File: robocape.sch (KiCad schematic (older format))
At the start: 16 parts

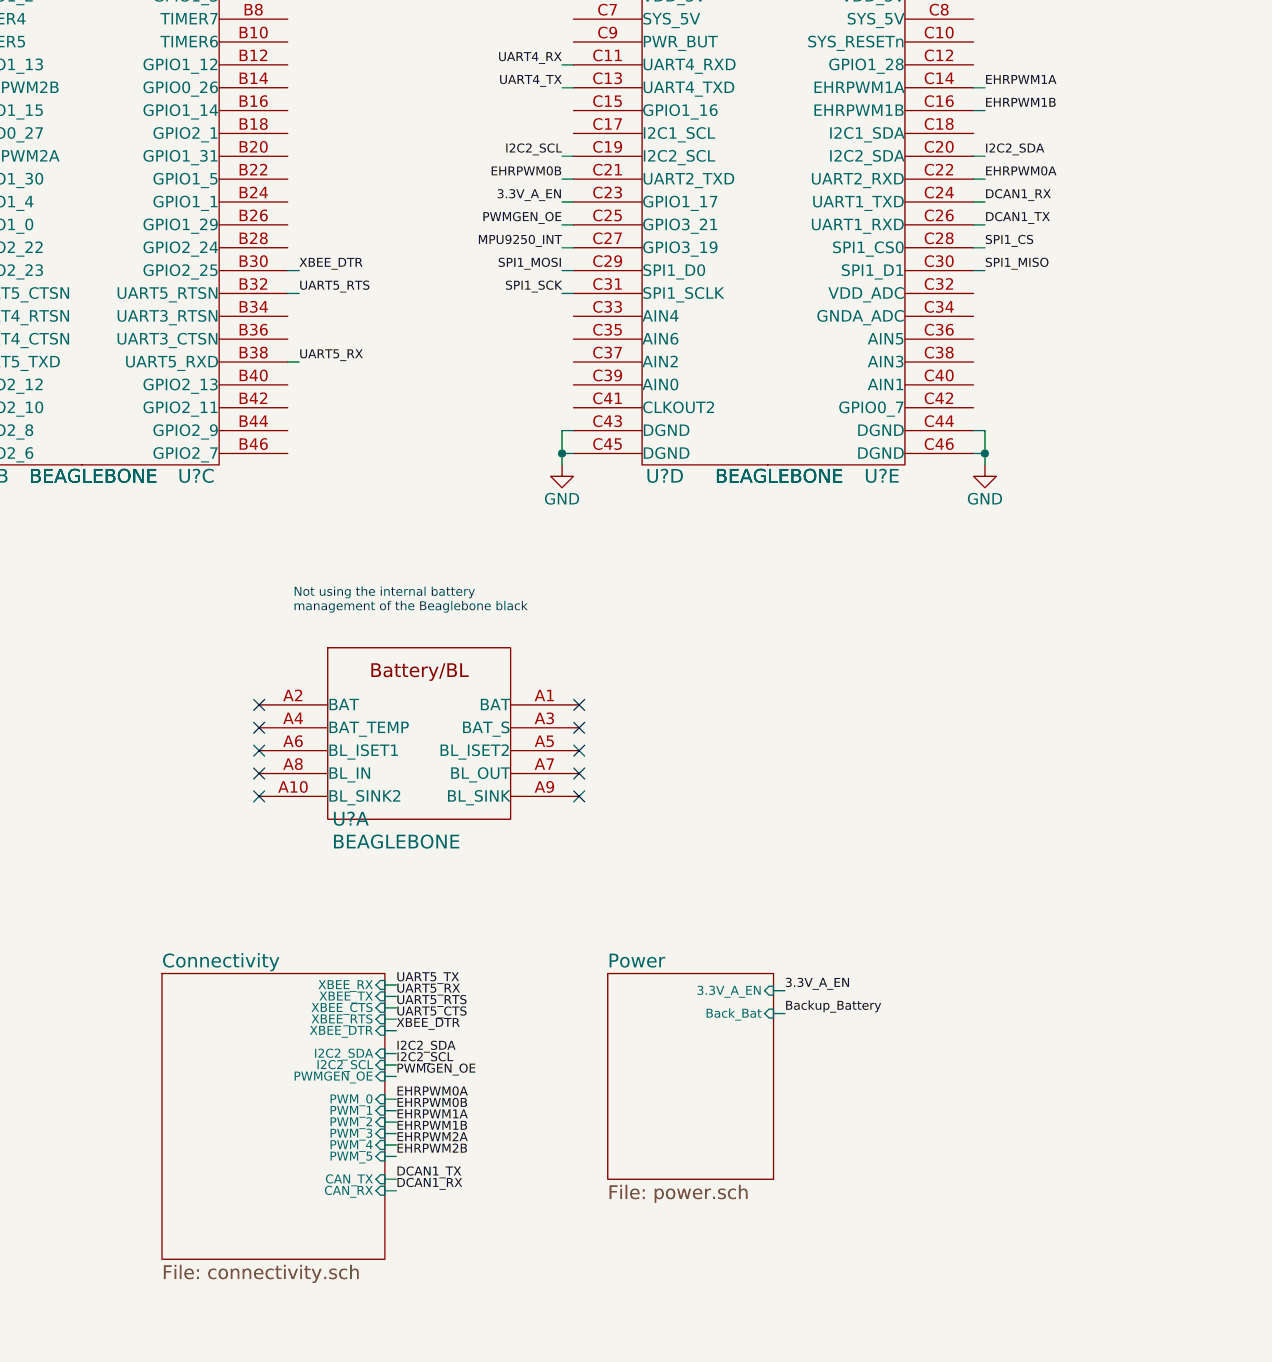
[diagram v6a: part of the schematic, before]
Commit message: Schematics: Additional connectors (ADC, I2C, UART)
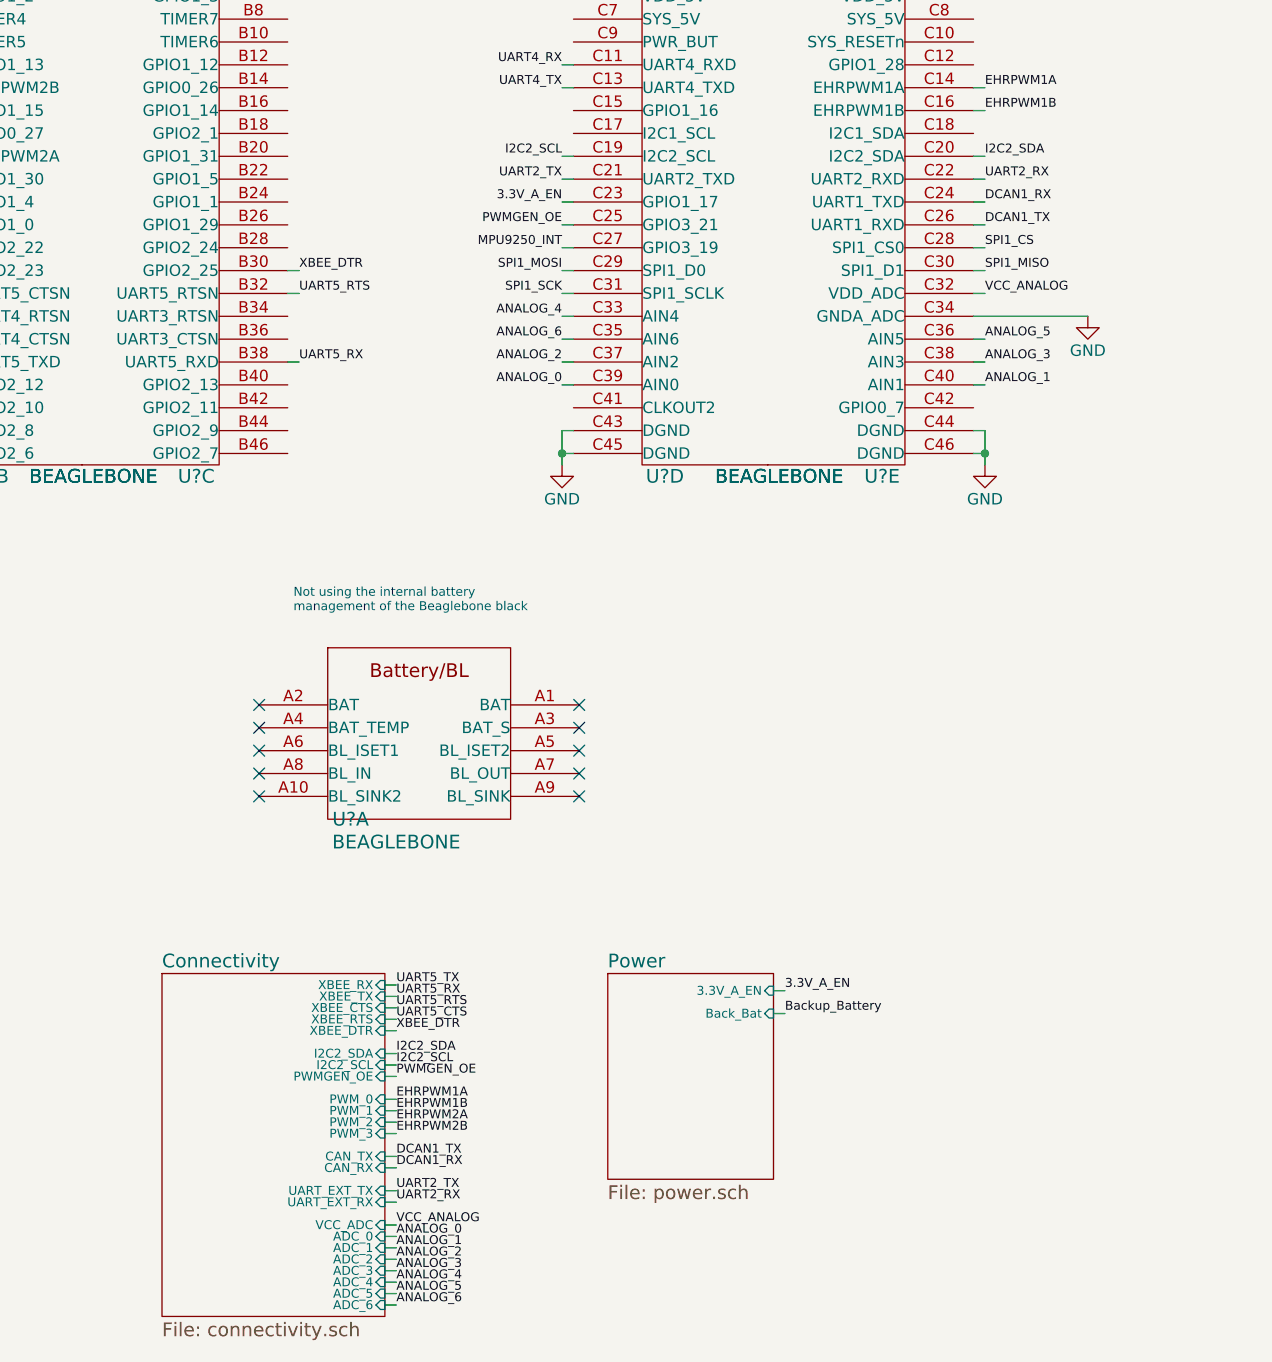
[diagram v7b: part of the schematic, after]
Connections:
- net GND: now also U?.C34 (GNDA_ADC)
- net ANALOG_4: now reaches U?.C33 (AIN4)
- net ANALOG_6: now reaches U?.C35 (AIN6)
- net ANALOG_2: now reaches U?.C37 (AIN2)
- net ANALOG_0: now reaches U?.C39 (AIN0)
- net VCC_ANALOG: now reaches U?.C32 (VDD_ADC)
- net ANALOG_5: now reaches U?.C36 (AIN5)
- net ANALOG_3: now reaches U?.C38 (AIN3)
- net ANALOG_1: now reaches U?.C40 (AIN1)
- net EHRPWM0A renamed UART2_RX
- net EHRPWM0B renamed UART2_TX

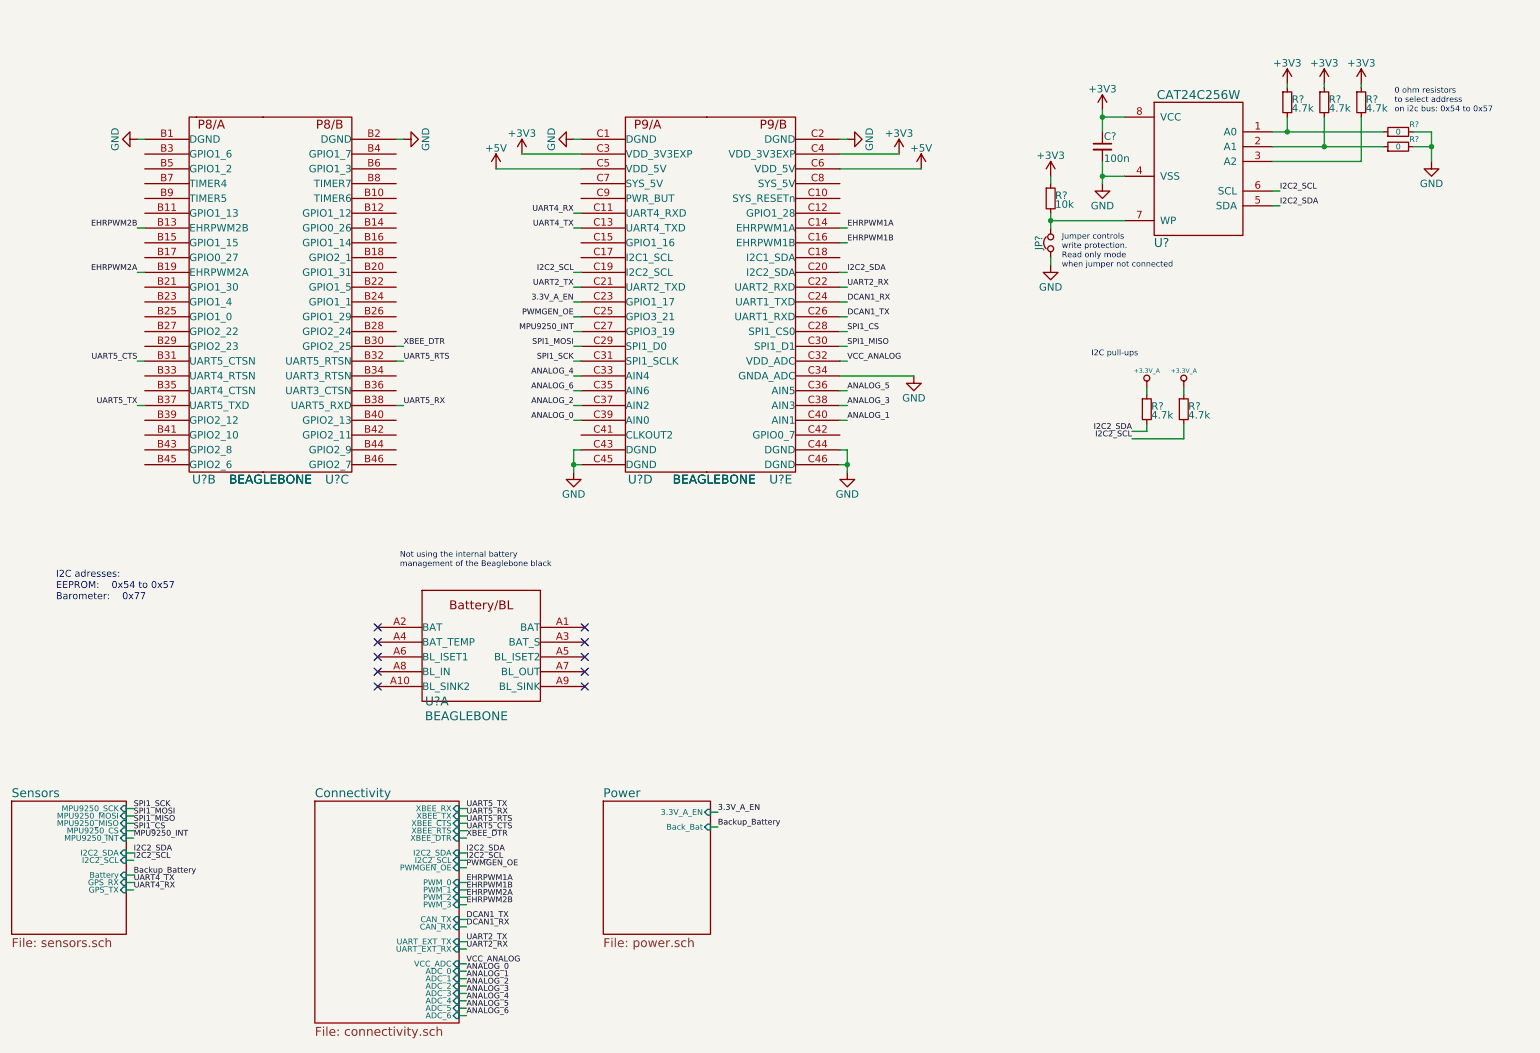
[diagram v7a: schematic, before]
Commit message: Schematics: RTC
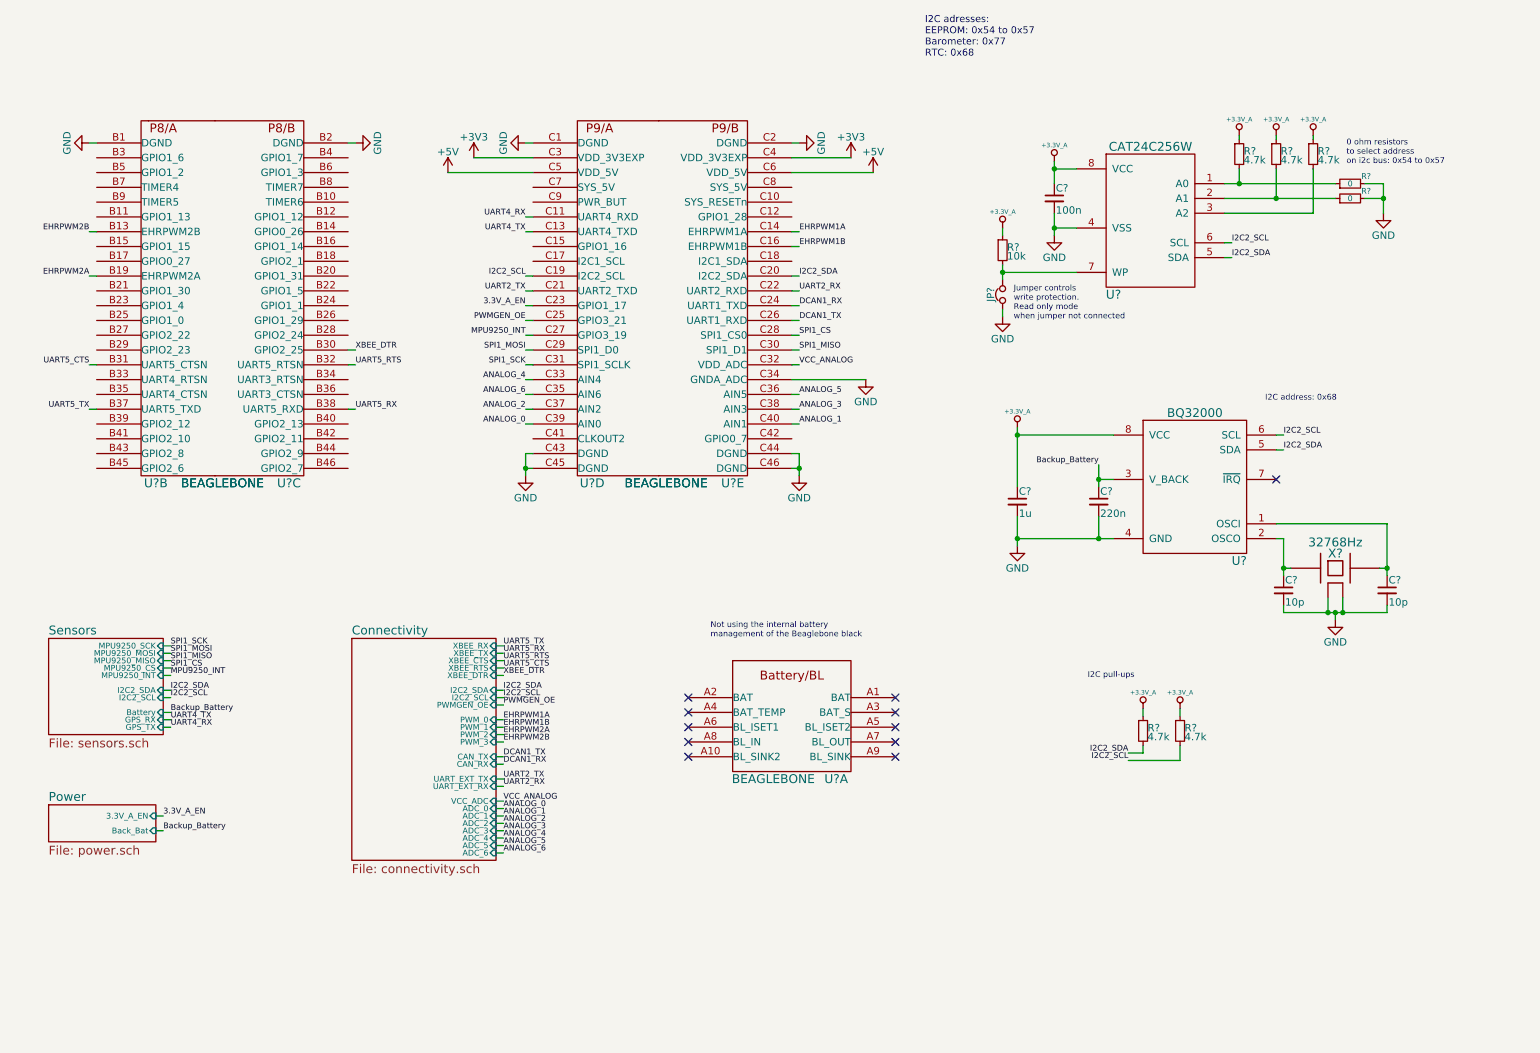
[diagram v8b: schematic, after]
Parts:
- added C?: 220n, symbol C_Small
- added C?: 1u, symbol C_Small
- added C? (x2): 10p, symbol C_Small
- added U?: BQ32000, symbol BQ32000
- added X?: 32768Hz, symbol XTAL-SMD-4-PADS
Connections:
- net +3.3V_A: now also C?.1, R?.1, R?.1, R?.1, R?.1, U?.8 (VCC), C?.1, U?.8 (VCC)
- net +3V3: no longer C?.1, R?.1, R?.1, R?.1, R?.1, U?.8 (VCC)
- net Backup_Battery: now also C?.1, U?.3 (V_BACK)
- net GND: now also C?.2, C?.2, C?.2, C?.2, U?.4 (GND), X?.2 (case), X?.4 (case)
- net I2C2_SCL: now also U?.6 (SCL)
- net I2C2_SDA: now also U?.5 (SDA)
- new net: C?.1, U?.1 (OSCI), X?.3
- new net: C?.1, U?.2 (OSCO), X?.1
- no-connect marks 10 -> 11
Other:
- note added: "I2C address: 0x68"
- note added: "I2C adresses:\nEEPROM: 0x54 to 0x57\nBarometer: 0x77\nRTC: 0x68"
- note removed: "I2C adresses:\nEEPROM: 0x54 to 0x57\nBarometer: 0x77\n"
- moved on the sheet: C?, JP?, R?, U?, U?A, U?B, U?C, U?D, U?E
